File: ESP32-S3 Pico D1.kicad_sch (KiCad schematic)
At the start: 0 parts

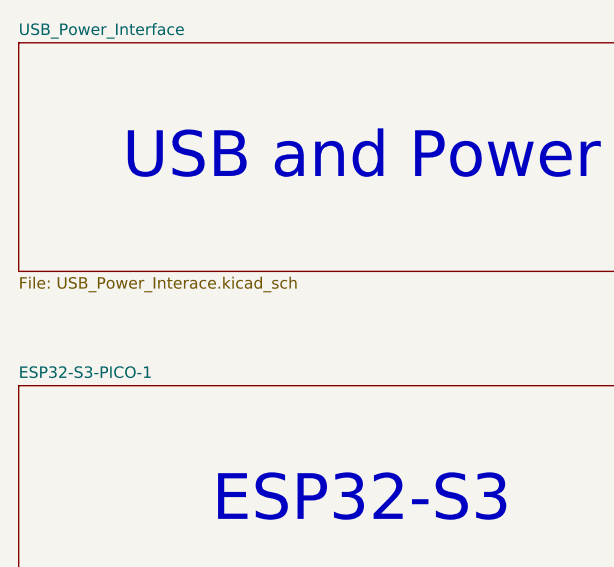
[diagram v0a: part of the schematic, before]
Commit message: streamlined routing by discarding legacy GPIO pinout compatibility. reduced Vin to Vcc and Vbus (no more +16V) includes CAN & Vehicle inputs (need to move to 2nd board, though) added wake-on-start by wiring Vacc to RTC_IO
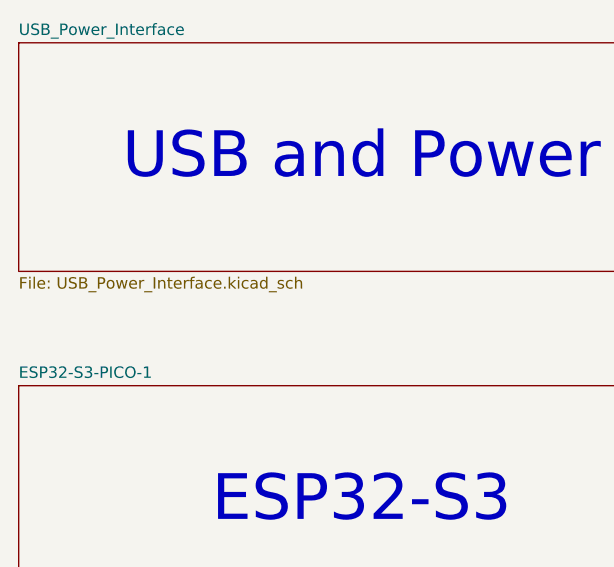
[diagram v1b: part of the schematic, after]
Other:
- sheet USB_Power_Interface: file USB_Power_Interace.kicad_sch -> USB_Power_Interface.kicad_sch
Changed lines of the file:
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@@
 			)
 		)
-		(property "Sheetfile" "USB_Power_Interace.kicad_sch"
+		(property "Sheetfile" "USB_Power_Interface.kicad_sch"
 			(at 50.8 64.0846 0)
 			(effects

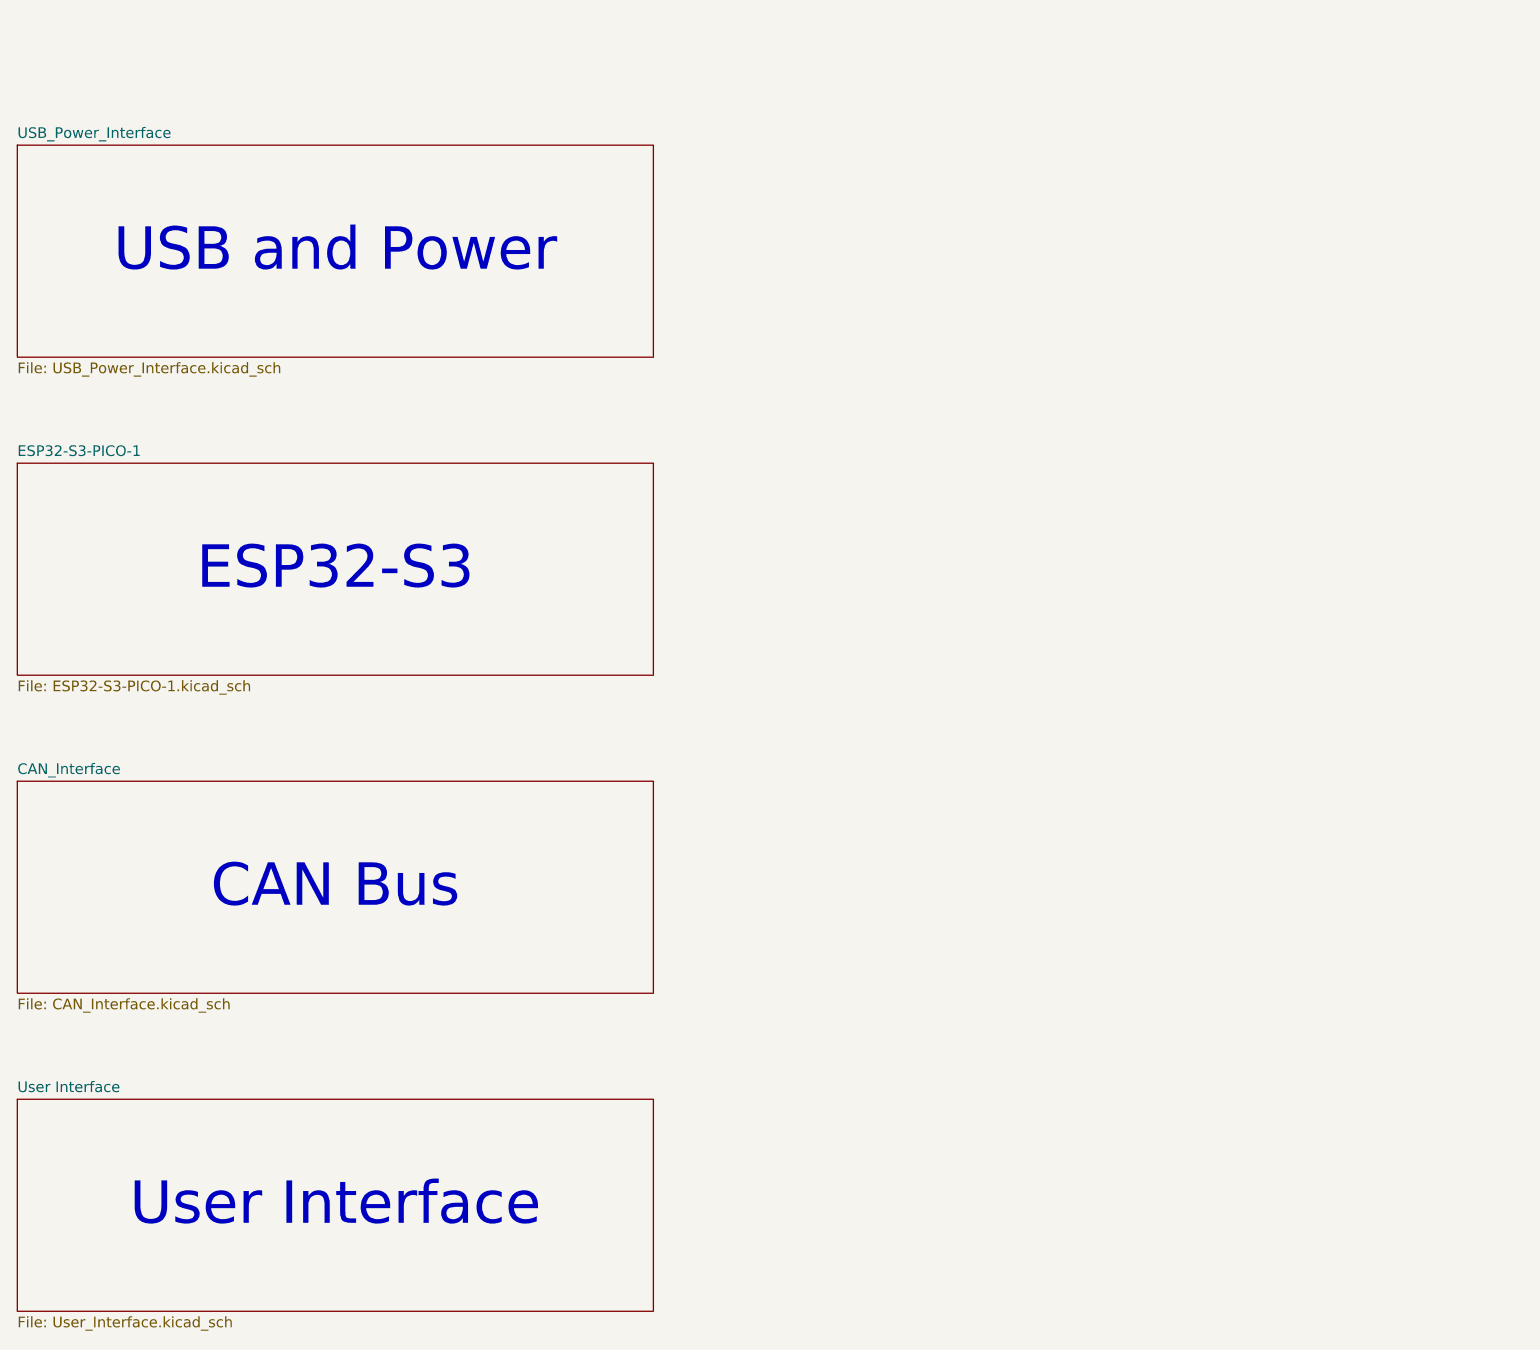
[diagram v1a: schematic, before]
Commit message: Update .gitignore, BOM-ESP32-S3 Pico D1.csv, CANBus_Interface.kicad_sch, and 14 more files
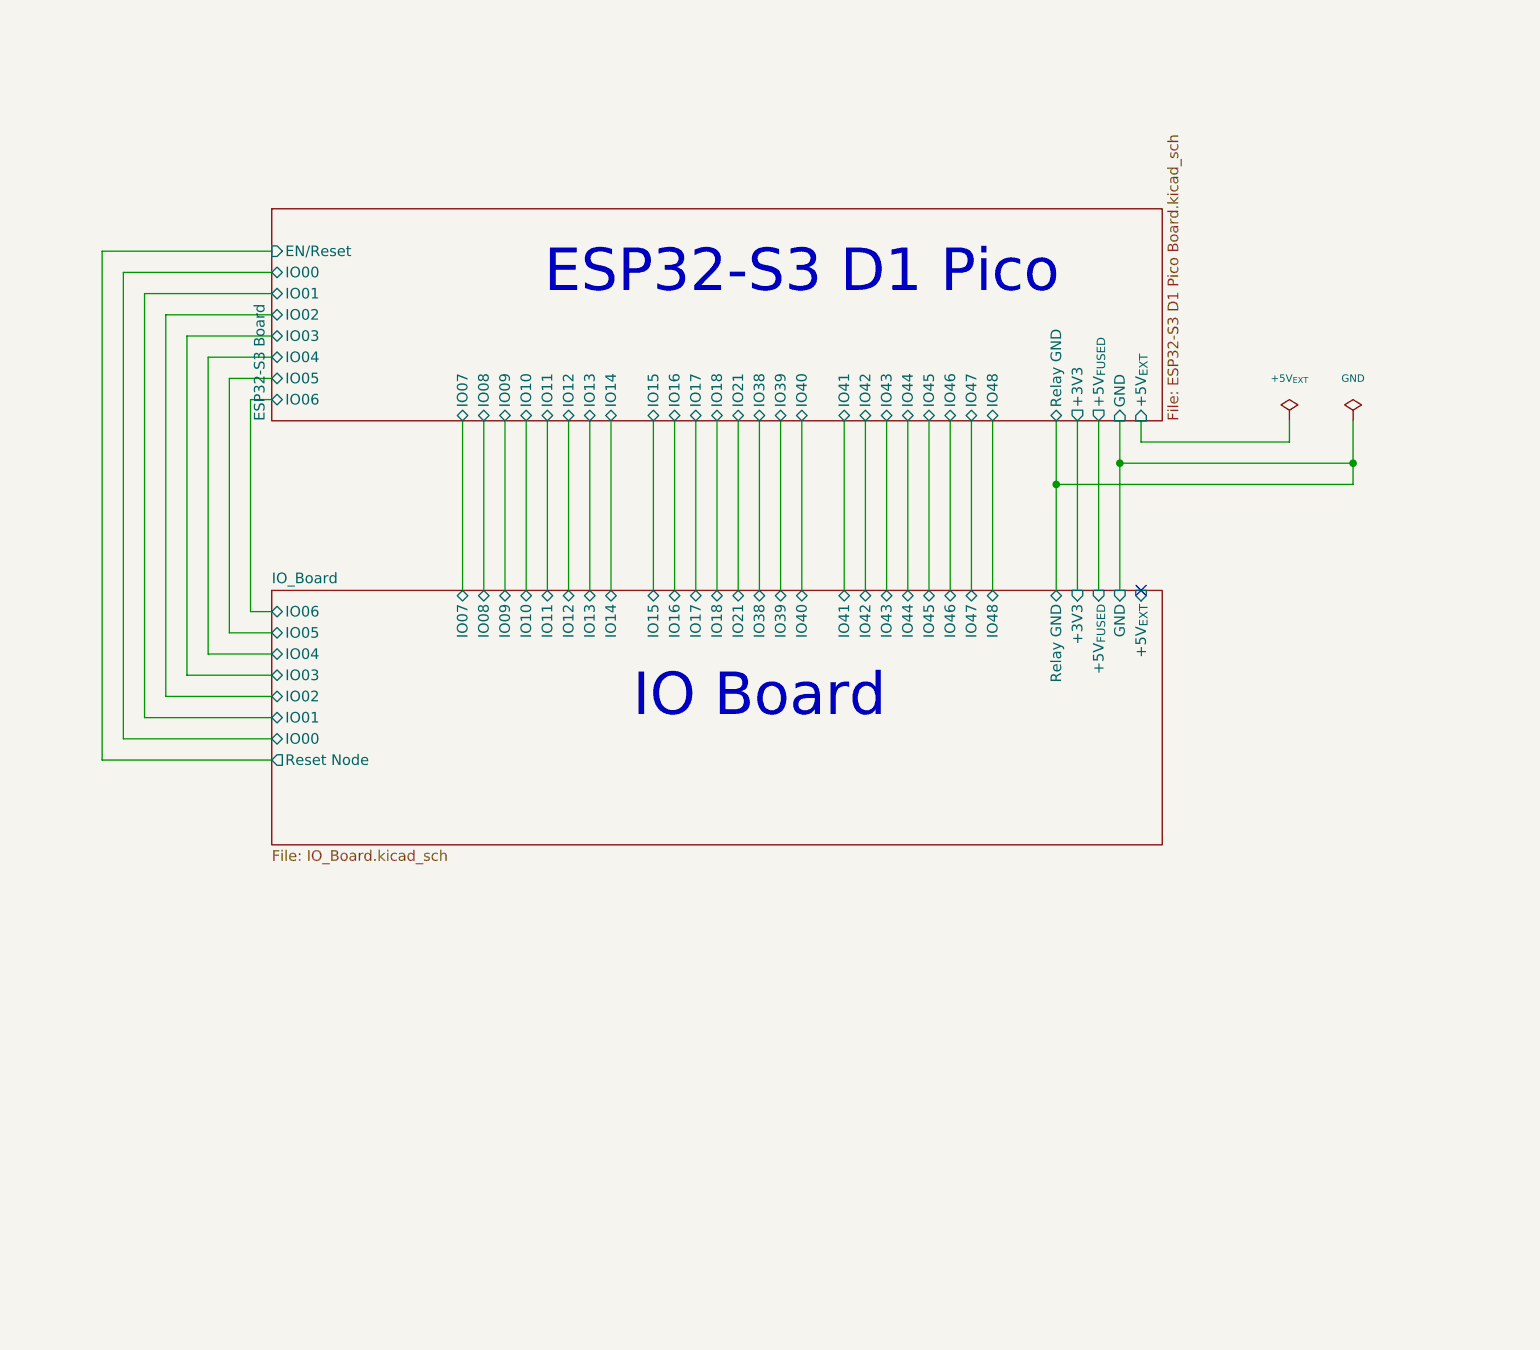
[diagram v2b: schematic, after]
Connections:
- no-connect marks 0 -> 1
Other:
- sheet CAN_Interface renamed IO_Board
- removed sheet ESP32-S3-PICO-1
- removed sheet USB_Power_Interface
- removed sheet User Interface
- added sheet ESP32-S3 Board (ESP32-S3 D1 Pico Board.kicad_sch)
- sheet IO_Board: file CAN_Interface.kicad_sch -> IO_Board.kicad_sch
- sheet IO_Board ports: added +3V3, +5V_{EXT}, +5V_{FUSED}, GND, IO00, IO01, IO02, IO03, IO04, IO05, IO06, IO07, IO08, IO09, IO10, IO11, IO12, IO13, IO14, IO15, IO16, IO17, IO18, IO21, IO38, IO39, IO40, IO41, IO42, IO43, IO44, IO45, IO46, IO47, IO48, Relay GND, Reset Node; removed none
- note added: "ESP32-S3 D1 Pico"
- note added: "IO Board"
- note removed: "CAN Bus"
- note removed: "ESP32-S3"
- note removed: "USB and Power"
- note removed: "User Interface"

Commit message: Update CANBus_Interface.kicad_sch, ESP32-S3 D1 Pico Board.kicad_sch, ESP32-S3 Pico D1.kicad_pcb, and 15 more files
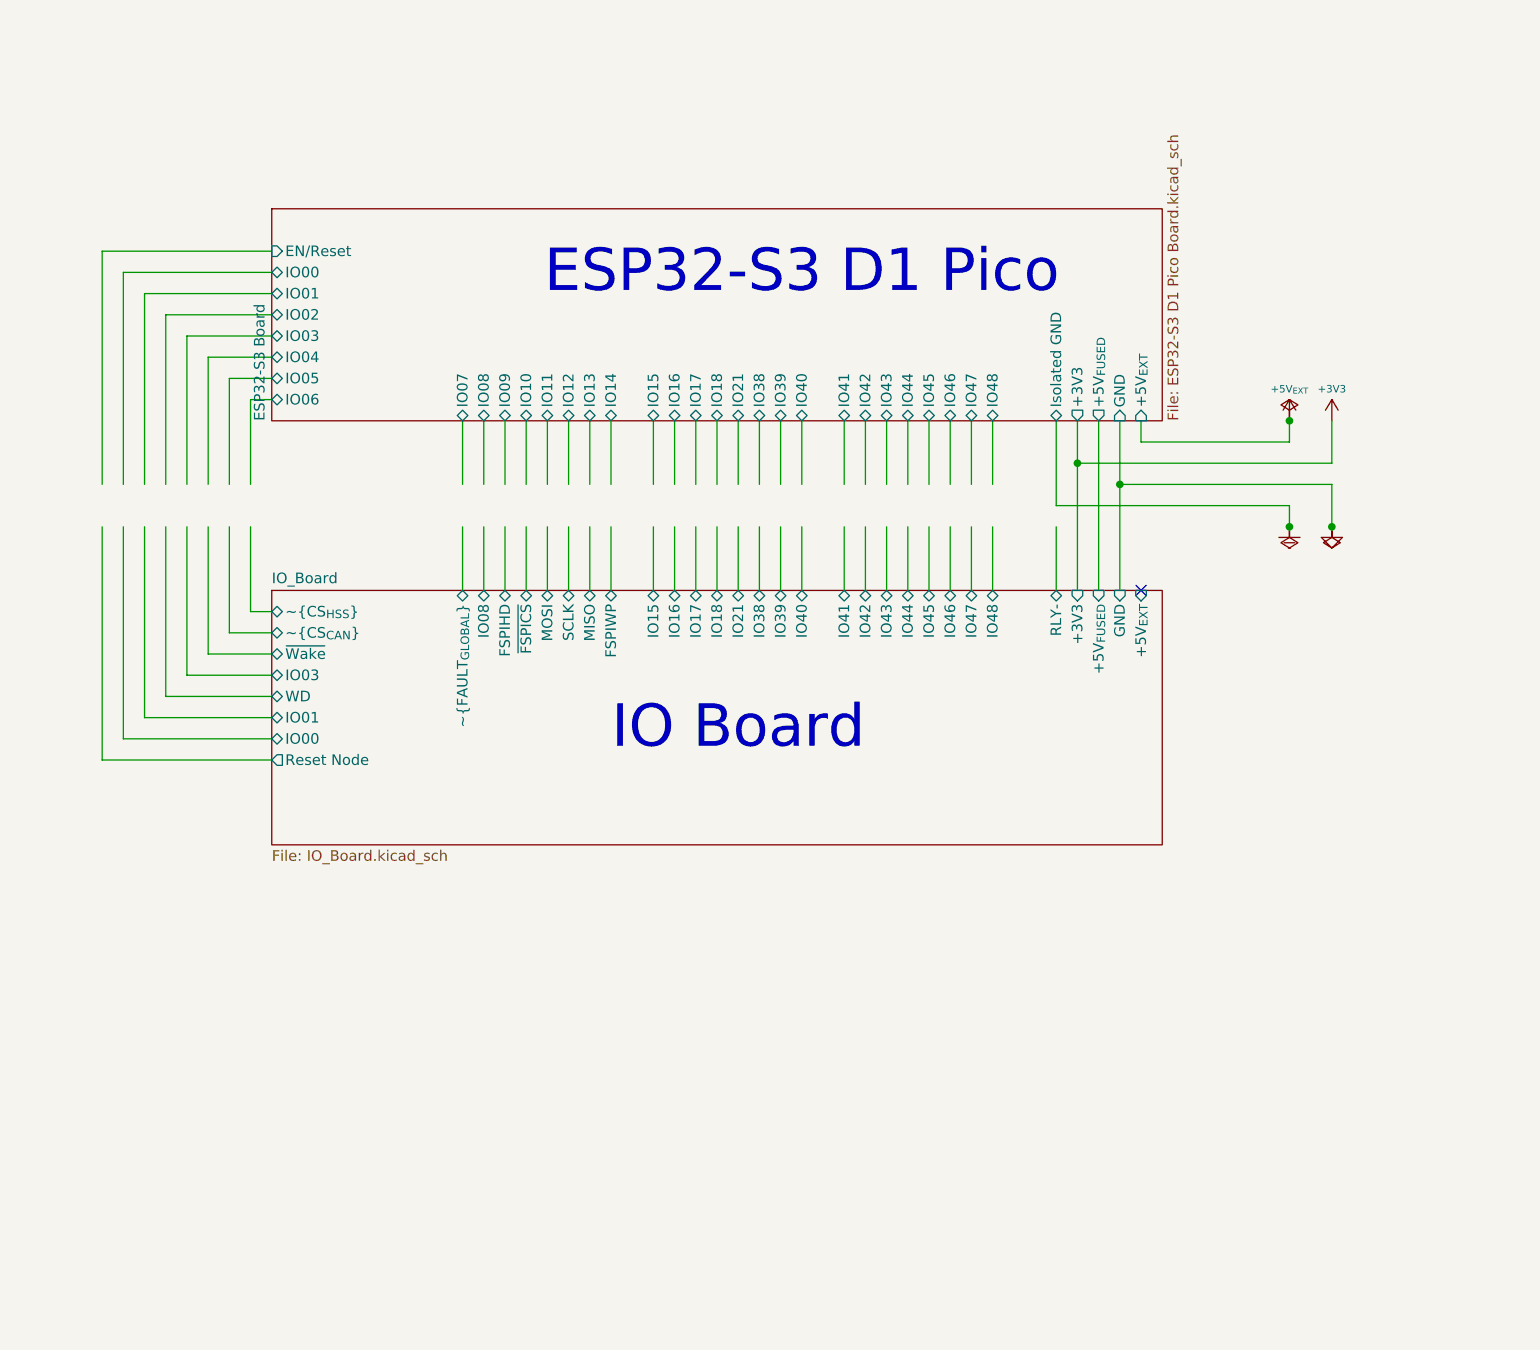
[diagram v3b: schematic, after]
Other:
- sheet ESP32-S3 Board ports: added Isolated GND; removed Relay GND
- sheet IO_Board ports: added FSPIHD, FSPIWP, MISO, MOSI, RLY-, SCLK, WD, ~{CS_{CAN}}, ~{CS_{HSS}}, ~{FAULT_{GLOBAL}}, ~{FSPICS}, ~{Wake}; removed IO02, IO04, IO05, IO06, IO07, IO09, IO10, IO11, IO12, IO13, IO14, Relay GND

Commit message: Update CAN_Interface.kicad_sch, ESP32-S3 D1 Pico Board.kicad_sch, ESP32-S3 Pico D1.kicad_pcb, and 5 more files
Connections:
- no-connect marks 1 -> 33
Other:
- removed sheet IO_Board
- sheet ESP32-S3 Board ports: added EN/~{Reset}; removed EN/Reset
- note removed: "IO Board"
